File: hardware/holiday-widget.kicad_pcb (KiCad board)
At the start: 4 copper layers, 108.4 x 65.8 mm, 155 parts, among them J2 UART, J33 Conn_ARM_JTAG_SWD_10, J4 BATTERY POWER, J5 VDC POWER, J7 Speaker, Q1 MMBT3906, Q10 MMBT3906, Q11 MMBT3906, Q12 MMBT3906, Q18 MMBT3906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

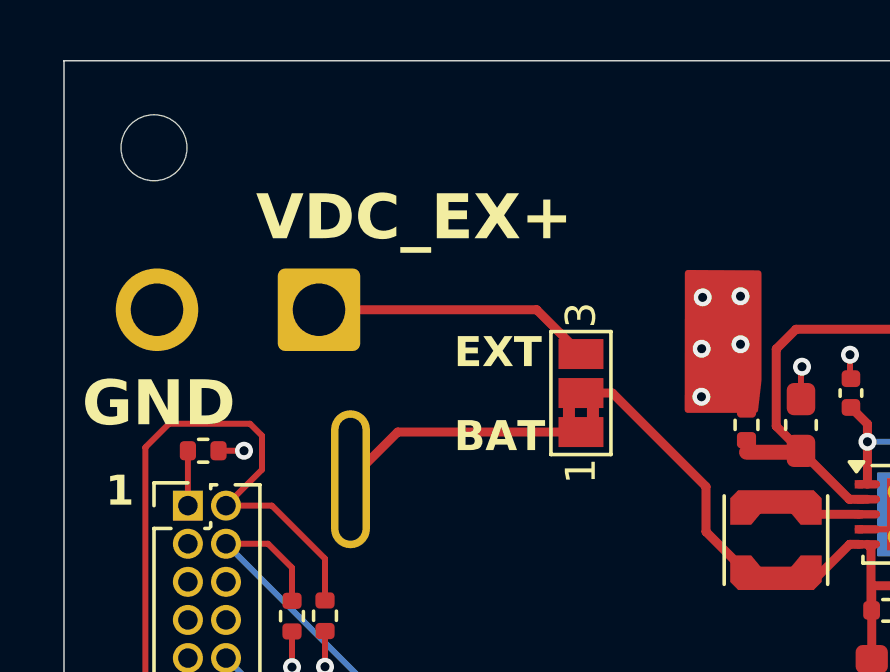
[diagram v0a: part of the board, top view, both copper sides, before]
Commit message: Remove external power connector
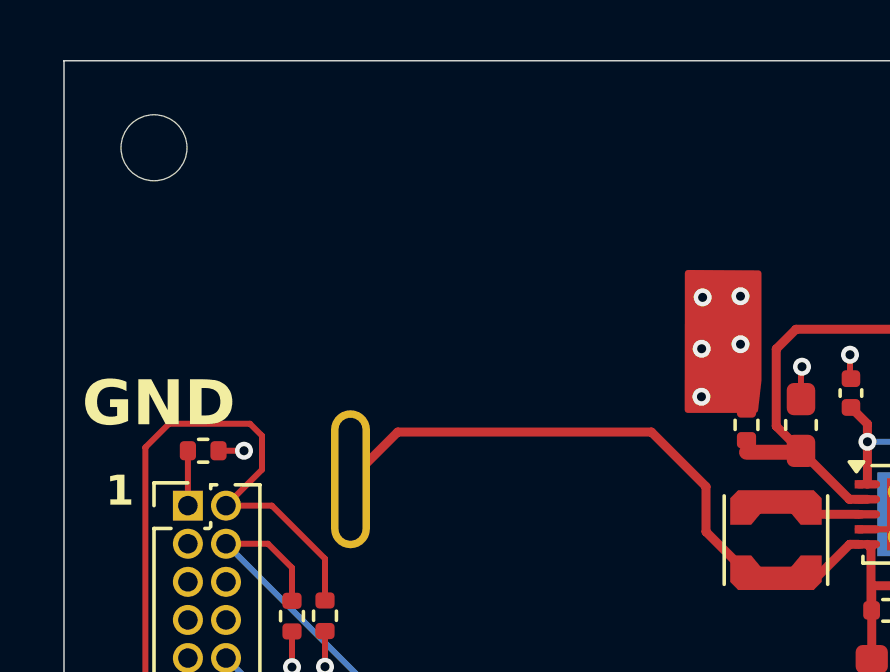
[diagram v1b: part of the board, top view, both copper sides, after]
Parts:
- removed J5: VDC POWER, Connector_Wire:SolderWire-1sqmm_1x02_P5.4mm_D1.4mm_OD2.7mm
- removed JP2: Jumper_3_Bridged12, Jumper:SolderJumper-3_P1.3mm_Bridged2Bar12_Pad1.0x1.5mm_NumberLabels
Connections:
- C23 pad 1: Net-(JP2-C) -> /VDC_BAT
- C9 pad 1: Net-(JP2-C) -> /VDC_BAT
- L1 pad 1: Net-(JP2-C) -> /VDC_BAT
- U2 pad 5: Net-(JP2-C) -> /VDC_BAT
- U2 pad 6: Net-(JP2-C) -> /VDC_BAT
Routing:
- net Net-(JP2-C): track 19.3 -> 0.00 mm
- net /VDC_BAT: track 8.33 -> 27.1 mm
- net /VDC_EX: track 9.34 -> 0.00 mm
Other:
- board text removed: "BAT"
- board text removed: "EXT"
- board text removed: "VDC_EX+"

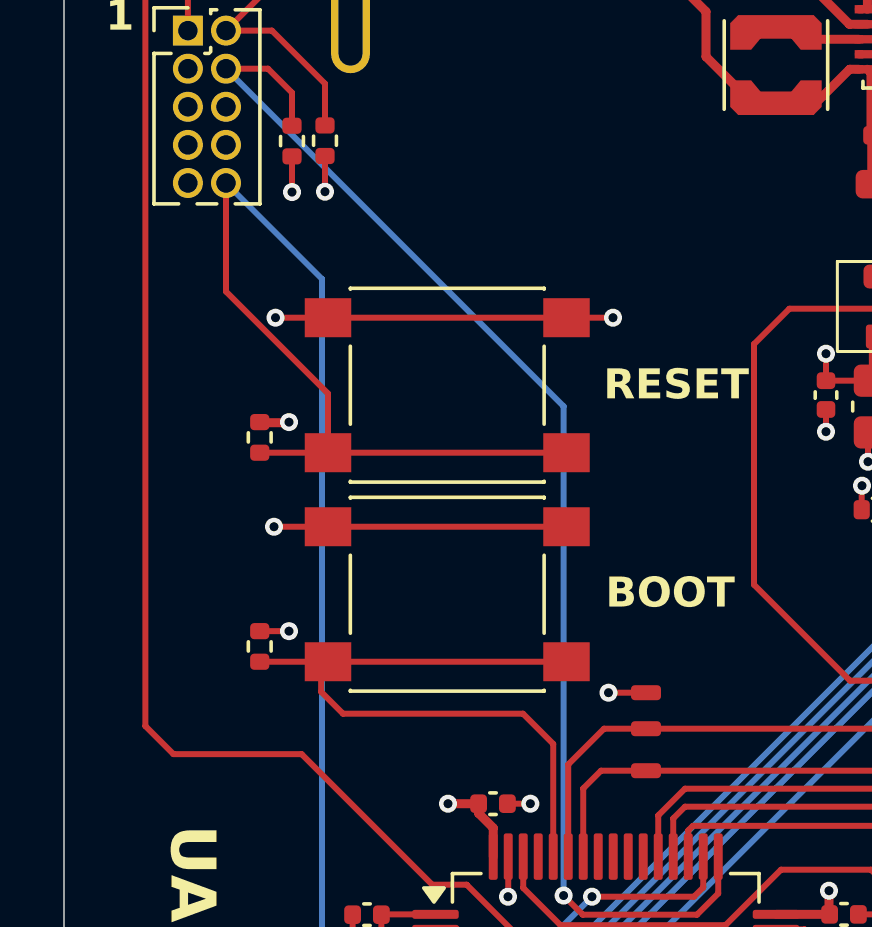
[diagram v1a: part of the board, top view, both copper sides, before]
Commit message: Replace buttons with jumper pads
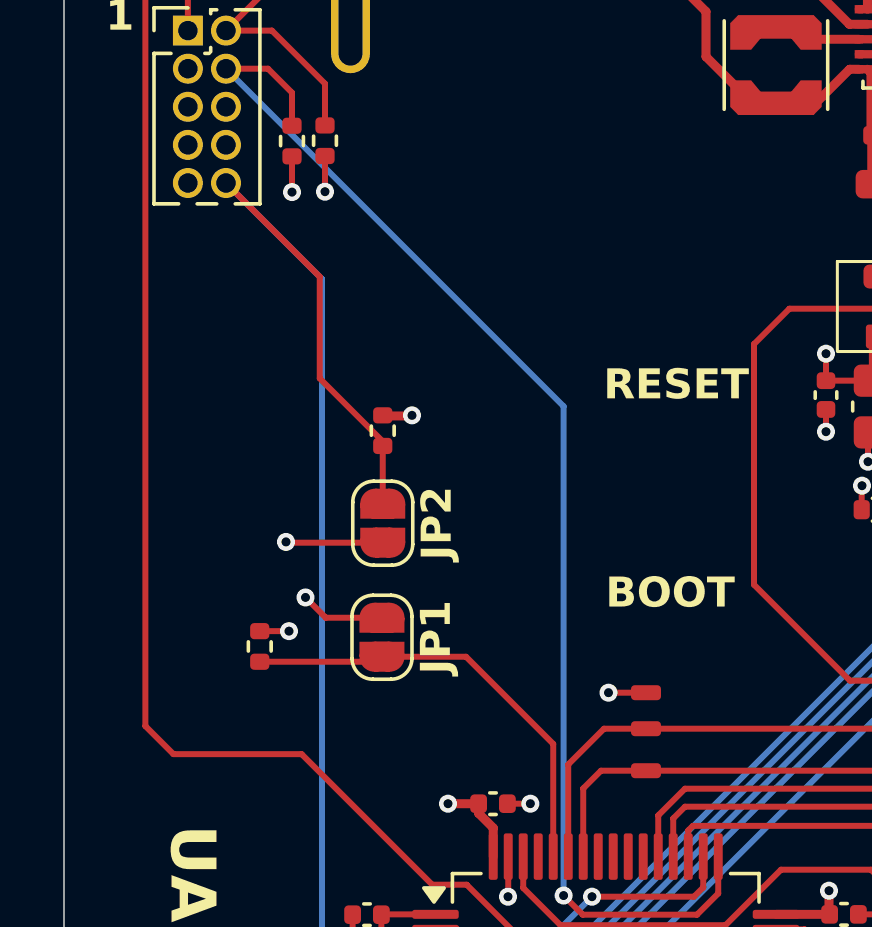
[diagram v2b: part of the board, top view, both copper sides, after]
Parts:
- removed SW1, SW4: SW_Push, Button_Switch_SMD:SW_Push_1P1T_NO_6x6mm_H9.5mm
- added JP1: Jumper_2_Small_Open, Jumper:SolderJumper-2_P1.3mm_Open_RoundedPad1.0x1.5mm, F.Cu at (137.8, 106.2)
- added JP2: Jumper_2_Small_Open, Jumper:SolderJumper-2_P1.3mm_Open_RoundedPad1.0x1.5mm, F.Cu at (137.8, 102.3)
- moved R1 4.11 mm to (137.8, 99.3)
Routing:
- net /mcu/BOOT: track 23.4 -> 14.8 mm
- net /GND: track 94.6 -> 86.6 mm, vias 64 -> 63
- net /mcu/nRST: track 53.1 -> 45.3 mm
- net /VDD: track 58.9 -> 52.1 mm

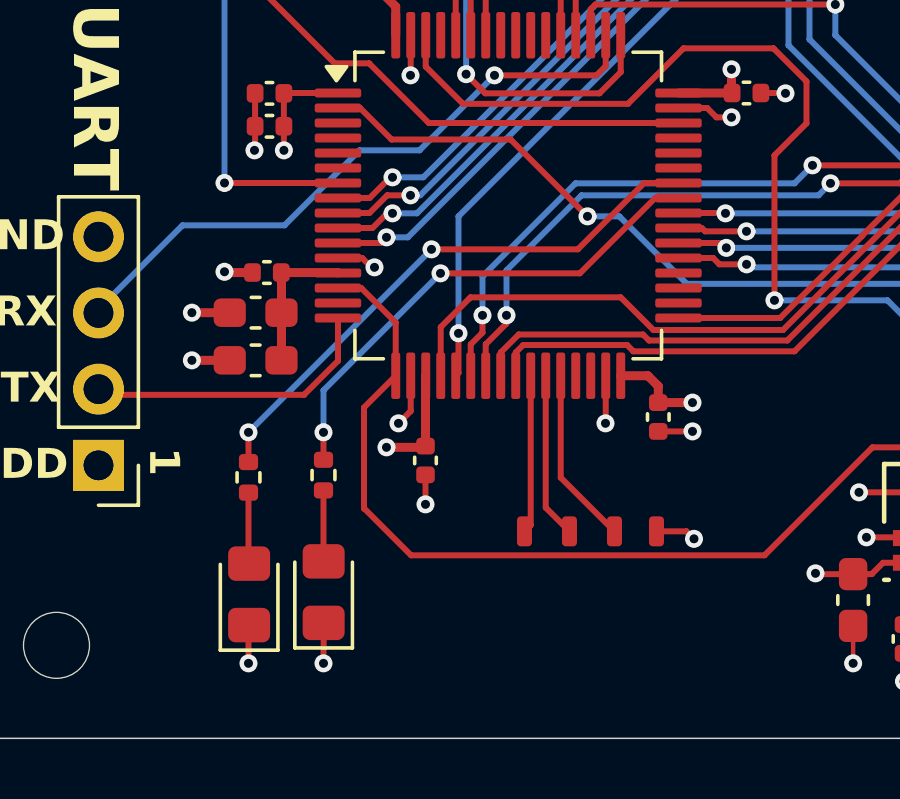
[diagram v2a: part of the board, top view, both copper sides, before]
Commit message: Remove status LEDs
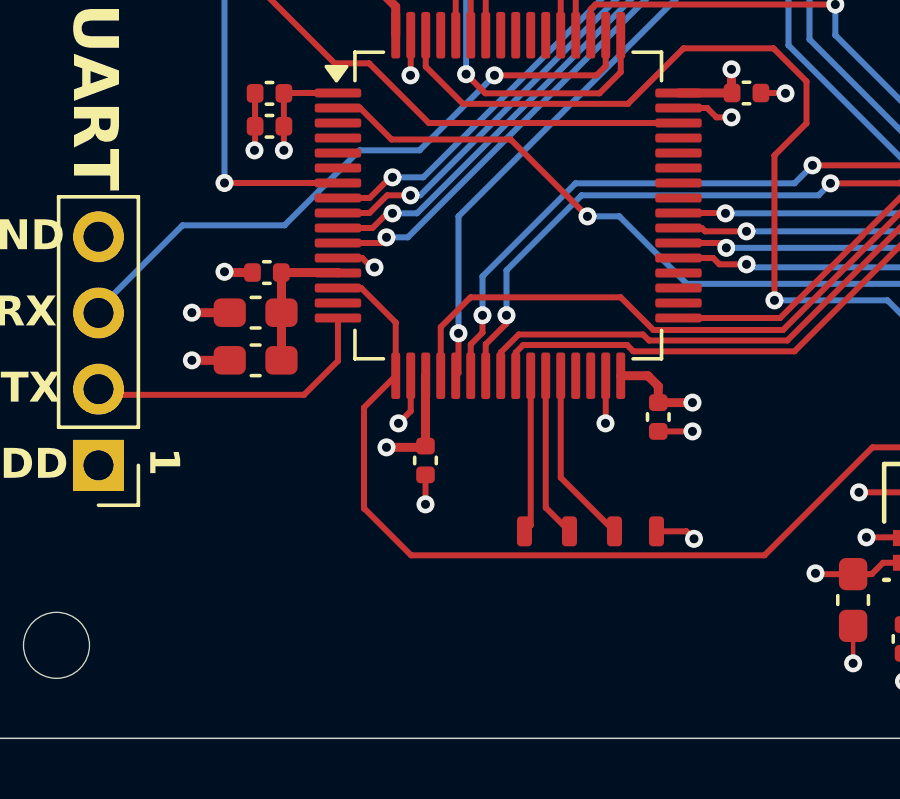
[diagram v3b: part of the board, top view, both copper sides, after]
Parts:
- removed D1, D2: LED, LED_SMD:LED_0805_2012Metric_Pad1.15x1.40mm_HandSolder
- removed R11, R12: 120, Resistor_SMD:R_0402_1005Metric
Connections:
- U1 pad 41: /mcu/STAT_LED0 -> unconnected-(U1-PA8-Pad41)
- U1 pad 42: /mcu/STAT_LED1 -> unconnected-(U1-PA9-Pad42)
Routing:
- net /mcu/STAT_LED1: track 18.8 -> 0.00 mm, vias 2 -> 0
- net /mcu/STAT_LED0: track 16.8 -> 0.00 mm, vias 2 -> 0
- net /GND: track 86.6 -> 84.0 mm, vias 63 -> 61
- net Net-(D1-A): track 2.36 -> 0.00 mm
- net Net-(D2-A): track 2.34 -> 0.00 mm

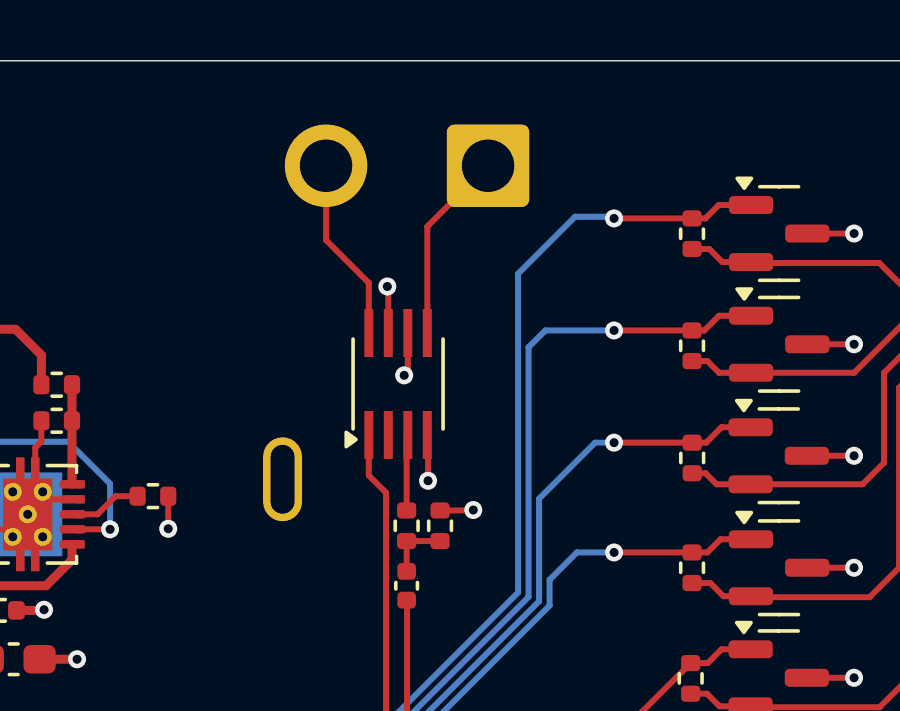
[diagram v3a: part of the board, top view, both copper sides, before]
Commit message: Add throughhole speaker
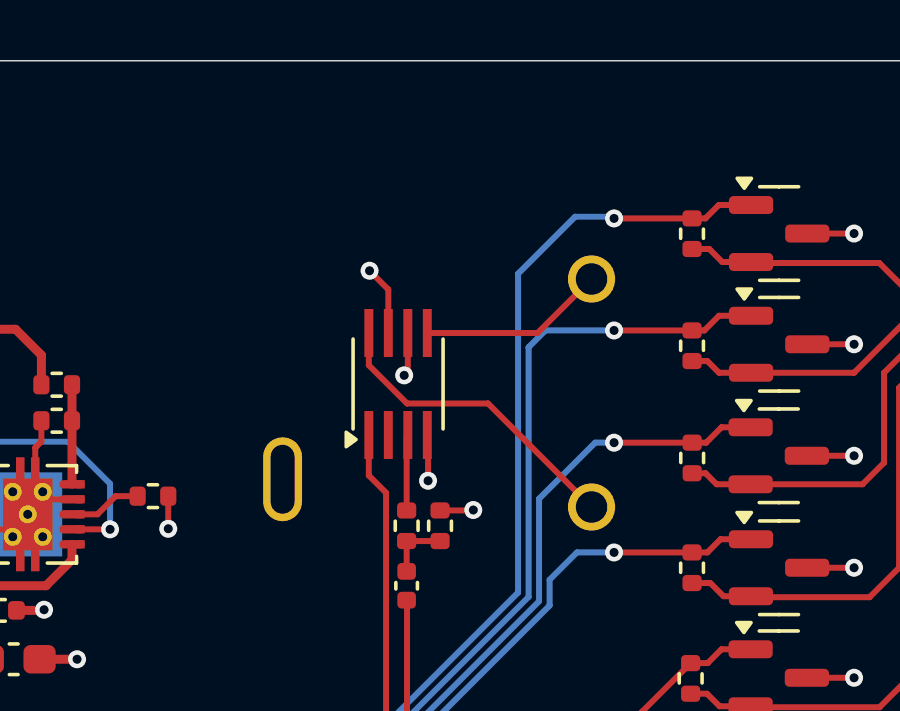
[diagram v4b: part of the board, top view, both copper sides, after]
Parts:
- J7: footprint Connector_Wire:SolderWire-1sqmm_1x02_P5.4mm_D1.4mm_OD2.7mm -> holiday-widget:SPKR_AST-01508MR-WT-R; moved to B.Cu
- moved J7 8.32 mm to (174.2, 82.2), turned to -90 degrees
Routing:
- net Net-(J7-Pin_2): track 6.17 -> 10.5 mm
- net /GND: track 84.0 -> 84.7 mm

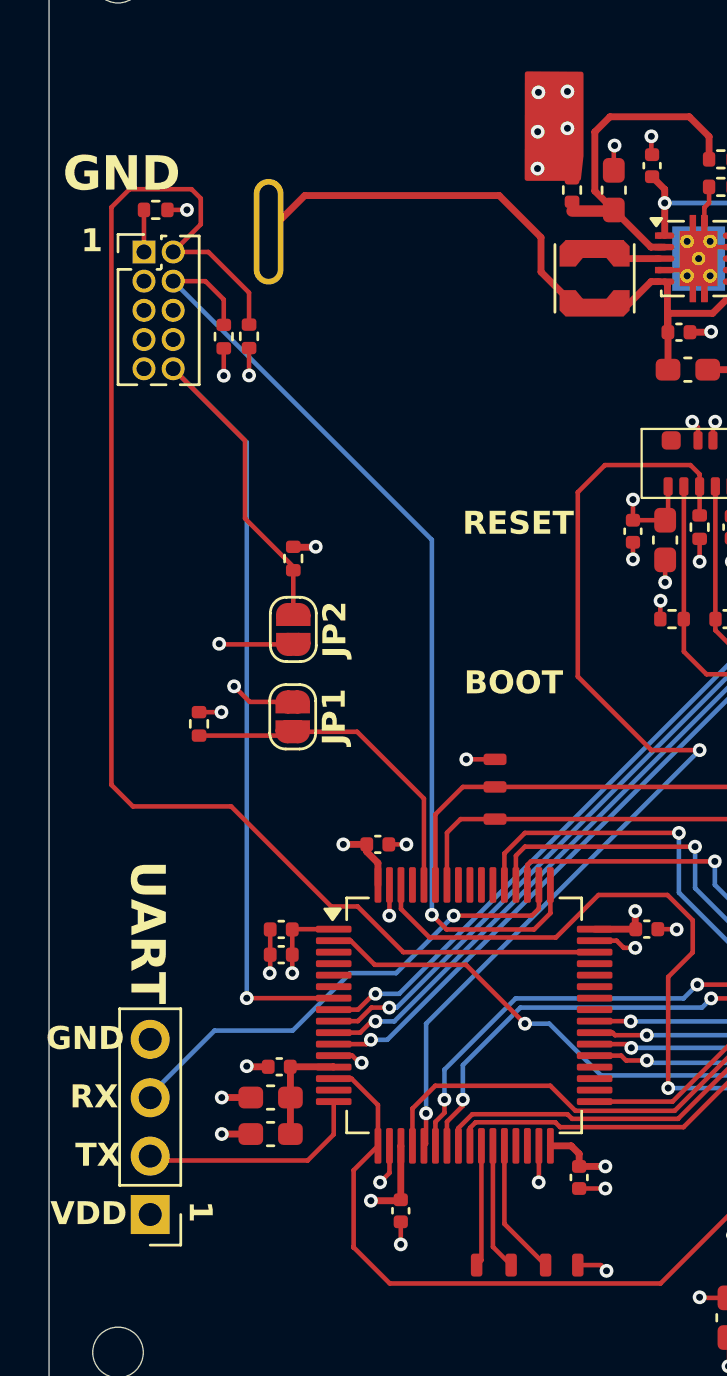
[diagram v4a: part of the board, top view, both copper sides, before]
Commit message: Remove some silkscreen text
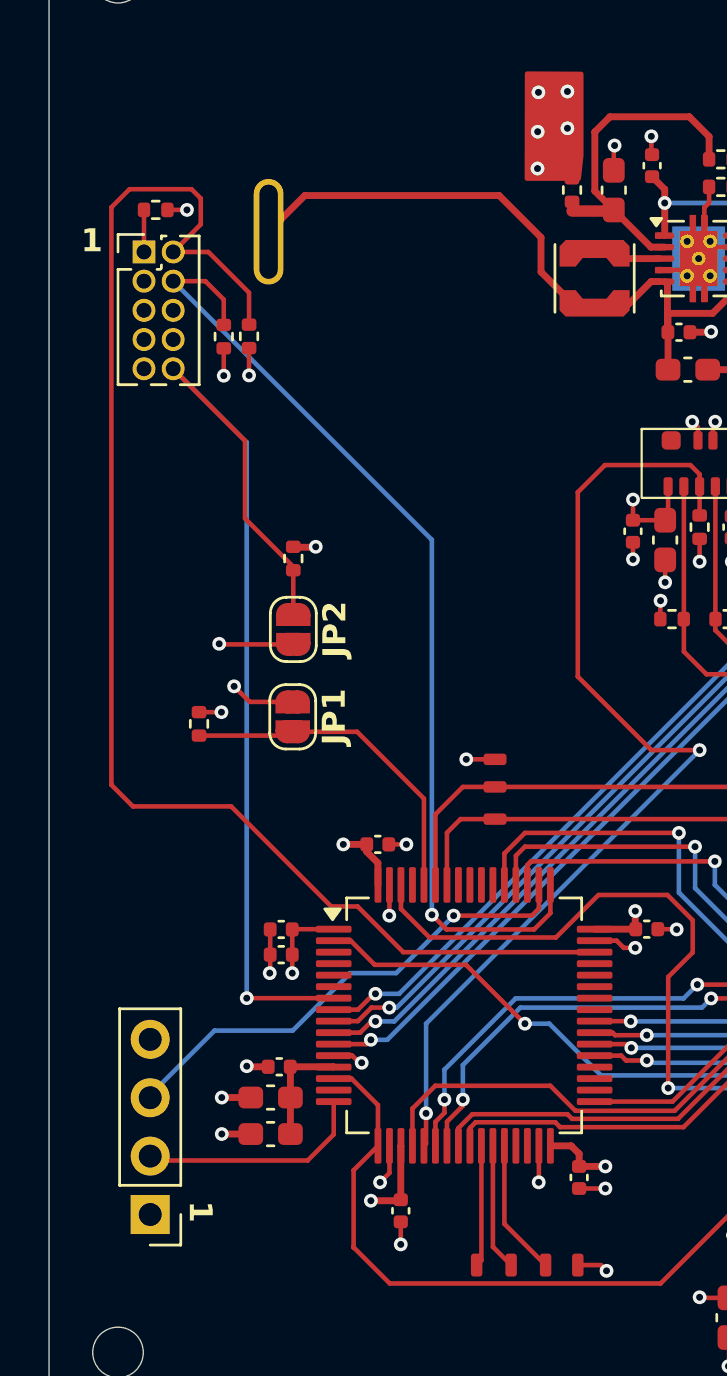
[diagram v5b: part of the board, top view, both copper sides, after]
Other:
- board text removed: "BOOT"
- board text removed: "GND"
- board text removed: "RESET"
- board text removed: "RX"
- board text removed: "TX"
- board text removed: "UART"
- board text removed: "VDD"
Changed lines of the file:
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@@
-		)
-	)
-	(gr_text "UART"
-		(at 130.6 112.4 270)
-		(layer "F.SilkS")
-		(effects
-			(font
-				(size 1.5 1.5)
-				(thickness 0.3)
-				(bold yes)
-			)
-			(justify left bottom)
 		)
 	)
@@
 		)
 	)
-	(gr_text "TX"
-		(at 128.338095 125.7995 0)
-		(layer "F.SilkS")
-		(effects
-			(font
-				(size 1 1)
-				(thickness 0.2)
-				(bold yes)
-			)
-			(justify left bottom)
-		)
-	)
 	(gr_text "1"
 		(at 128.583289 86.020074 0)
-		(layer "F.SilkS")
-		(effects
-			(font
-				(size 1 1)
-				(thickness 0.2)
-				(bold yes)
-			)
-			(justify left bottom)
-		)
-	)
-	(gr_text "RX"
-		(at 128.1 123.2595 0)
 		(layer "F.SilkS")
 		(effects
@@
 		)
 	)
-	(gr_text "BOOT"
-		(at 145.25 105.25 0)
-		(layer "F.SilkS")
-		(effects
-			(font
-				(size 1 1)
-				(thickness 0.2)
-				(bold yes)
-			)
-			(justify left bottom)
-		)
-	)
-	(gr_text "VDD"
-		(at 127.257143 128.3395 0)
-		(layer "F.SilkS")
-		(effects
-			(font
-				(size 1 1)
-				(thickness 0.2)
-				(bold yes)
-			)
-			(justify left bottom)
-		)
-	)
-	(gr_text "GND"
-		(at 127.066667 120.7195 0)
-		(layer "F.SilkS")
-		(effects
-			(font
-				(size 1 1)
-				(thickness 0.2)
-				(bold yes)
-			)
-			(justify left bottom)
-		)
-	)
-	(gr_text "GND"
-		(at 127.8 83.4 0)
-		(layer "F.SilkS")
-		(effects
-			(font
-				(size 1.5 1.5)
-				(thickness 0.3)
-				(bold yes)
-			)
-			(justify left bottom)
-		)
-	)
-	(gr_text "RESET"
-		(at 145.181878 98.310174 0)
-		(layer "F.SilkS")
-		(effects
-			(font
-				(size 1 1)
-				(thickness 0.2)
-				(bold yes)
-			)
-			(justify left bottom)
-		)
-	)
